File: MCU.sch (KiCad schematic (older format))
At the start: 10 parts, among them U2 TPS70925, U3 STM32L011F4Ux

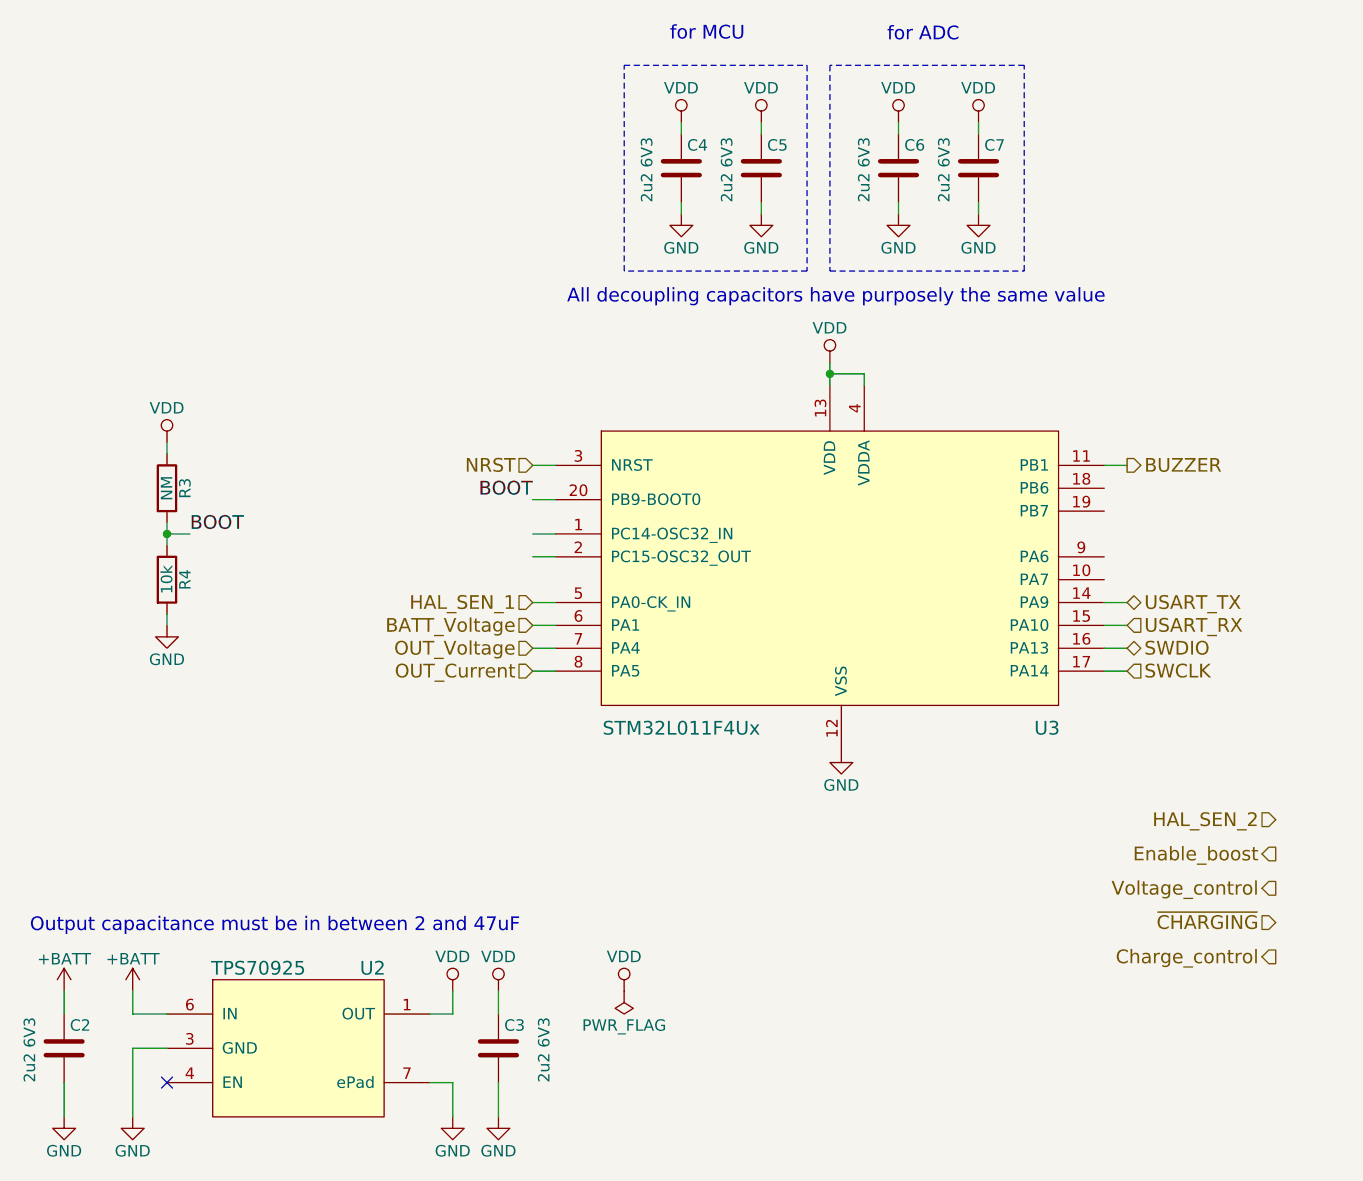
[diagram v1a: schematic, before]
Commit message: Updated MCU pinout
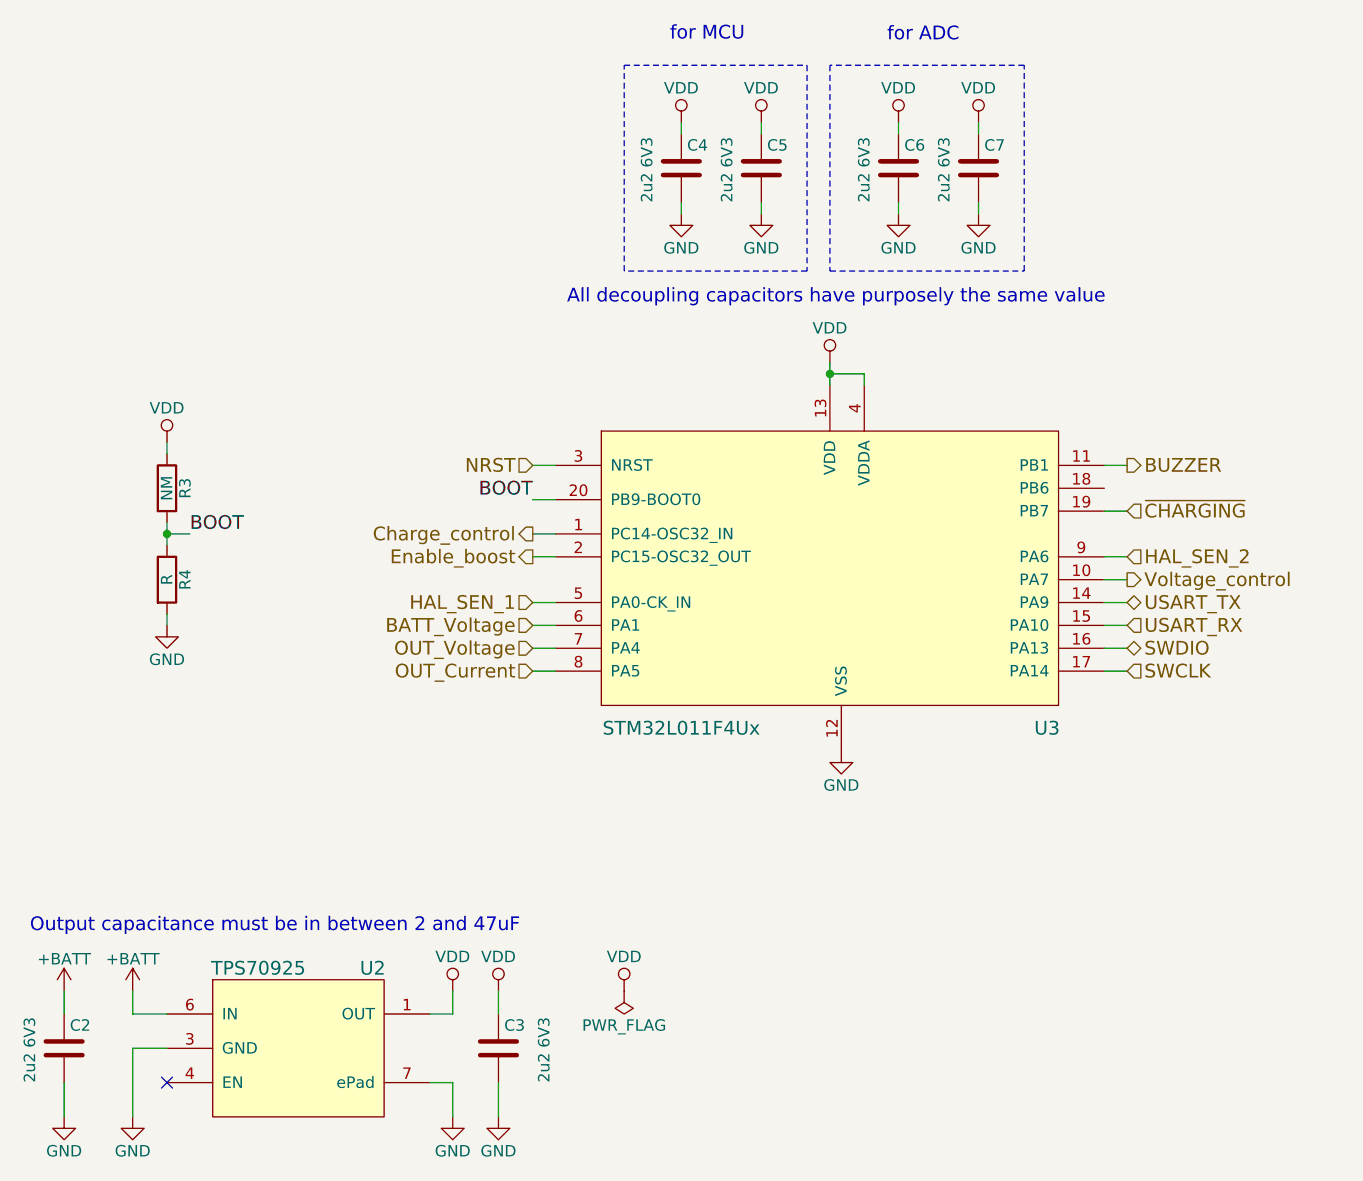
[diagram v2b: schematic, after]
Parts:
- R4: value 10k -> R
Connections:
- wire segments 40 -> 43
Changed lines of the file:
@@
 P 3200 4200
 F 0 "R4" V 3280 4200 50  0000 C CNN
-F 1 "10k" V 3200 4200 50  0000 C CNN
+F 1 "R" V 3200 4200 50  0000 C CNN
 F 2 "" V 3130 4200 50  0001 C CNN
 F 3 "" H 3200 4200 50  0001 C CNN
@@
 Wire Wire Line
 	4800 4300 4900 4300
-Text HLabel 8050 5250 0    60   Input ~ 0
+Text HLabel 7400 4100 2    60   Input ~ 0
 HAL_SEN_2
 $Comp
@@
 Text HLabel 7400 3700 2    60   Output ~ 0
 BUZZER
-Text HLabel 8050 5550 0    60   Output ~ 0
+Text HLabel 7400 4200 2    60   Output ~ 0
 Voltage_control
-Text HLabel 8050 5400 0    60   Output ~ 0
+Text HLabel 4800 4100 0    60   Output ~ 0
 Enable_boost
 Text HLabel 4800 4500 0    60   Input ~ 0
@@
 Text Notes 4950 3000 0    60   ~ 0
 All decoupling capacitors have purposely the same value\n
-Text HLabel 8050 5700 0    60   Input ~ 0
+Text HLabel 7400 3900 2    60   Input ~ 0
 ~CHARGING
-Text HLabel 8050 5850 0    60   Output ~ 0
+Text HLabel 4800 4000 0    60   Output ~ 0
 Charge_control
+Wire Wire Line
+	7300 4200 7400 4200
+Wire Wire Line
+	7300 4100 7400 4100
+Wire Wire Line
+	7300 3900 7400 3900
 $EndSCHEMATC

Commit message: Simplified schematic, changed pinout
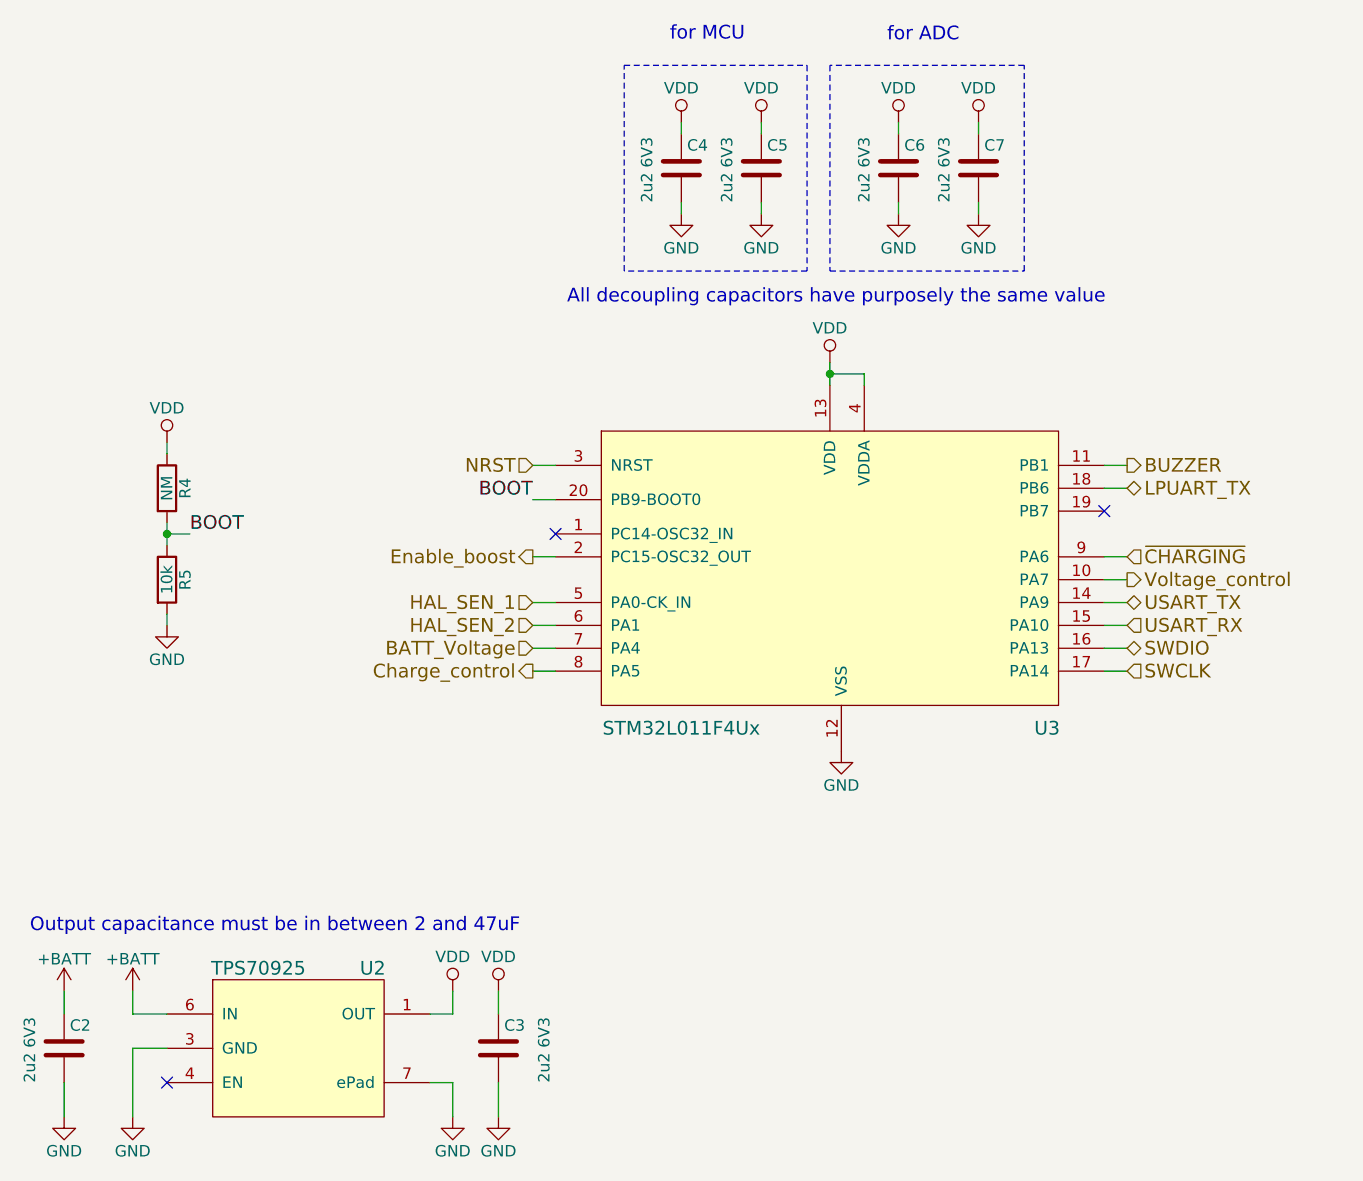
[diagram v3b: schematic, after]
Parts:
- C2, C3, C4, C5, C6, C7: footprint (none) -> Capacitors_SMD:C_0402
- R4: renamed from R3; footprint (none) -> Resistors_SMD:R_0402
- R5: renamed from R4; value R -> 10k; footprint (none) -> Resistors_SMD:R_0402
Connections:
- net OUT_Current is gone; now on net Charge_control: U3.8 (PA5)
- net OUT_Voltage is gone; now on net BATT_Voltage: U3.7 (PA4)
- net BATT_Voltage: no longer U3.6 (PA1)
- net Charge_control: no longer U3.1 (PC14-OSC32_IN)
- net HAL_SEN_2: now also U3.6 (PA1); no longer U3.9 (PA6)
- net ~CHARGING: now also U3.9 (PA6); no longer U3.19 (PB7)
- net LPUART_TX: now reaches U3.18 (PB6)
- no-connect marks 1 -> 3
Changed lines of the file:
@@
 $EndDescr
 $Comp
-L VDD #PWR30
+L VDD #PWR012
 U 1 1 5A9B30A9
 P 6100 3250
-F 0 "#PWR30" H 6100 3100 50  0001 C CNN
+F 0 "#PWR012" H 6100 3100 50  0001 C CNN
 F 1 "VDD" H 6100 3400 50  0000 C CNN
 F 2 "" H 6100 3250 50  0001 C CNN
@@
 Connection ~ 6100 3300
 $Comp
-L GND #PWR31
+L GND #PWR013
 U 1 1 5A9B30B3
 P 6150 4950
-F 0 "#PWR31" H 6150 4700 50  0001 C CNN
+F 0 "#PWR013" H 6150 4700 50  0001 C CNN
 F 1 "GND" H 6150 4800 50  0000 C CNN
 F 2 "" H 6150 4950 50  0001 C CNN
@@
 $EndComp
 $Comp
-L GND #PWR18
+L GND #PWR014
 U 1 1 5A9B3148
 P 3050 6550
-F 0 "#PWR18" H 3050 6300 50  0001 C CNN
+F 0 "#PWR014" H 3050 6300 50  0001 C CNN
 F 1 "GND" H 3050 6400 50  0000 C CNN
 F 2 "" H 3050 6550 50  0001 C CNN
@@
 NoConn ~ 3200 6400
 $Comp
-L GND #PWR22
+L GND #PWR015
 U 1 1 5A9B3188
 P 4450 6550
-F 0 "#PWR22" H 4450 6300 50  0001 C CNN
+F 0 "#PWR015" H 4450 6300 50  0001 C CNN
 F 1 "GND" H 4450 6400 50  0000 C CNN
 F 2 "" H 4450 6550 50  0001 C CNN
@@
 	4450 6400 4450 6550
 $Comp
-L VDD #PWR21
+L VDD #PWR016
 U 1 1 5A9B31B3
 P 4450 6000
-F 0 "#PWR21" H 4450 5850 50  0001 C CNN
+F 0 "#PWR016" H 4450 5850 50  0001 C CNN
 F 1 "VDD" H 4450 6150 50  0000 C CNN
 F 2 "" H 4450 6000 50  0001 C CNN
@@
 	4450 6100 4350 6100
 $Comp
-L +BATT #PWR17
+L +BATT #PWR017
 U 1 1 5A9B31F8
 P 3050 6000
-F 0 "#PWR17" H 3050 5850 50  0001 C CNN
+F 0 "#PWR017" H 3050 5850 50  0001 C CNN
 F 1 "+BATT" H 3050 6140 50  0000 C CNN
 F 2 "" H 3050 6000 50  0001 C CNN
@@
 F 0 "C3" H 4675 6350 50  0000 L CNN
 F 1 "2u2 6V3" V 4850 6100 50  0000 L CNN
-F 2 "" H 4688 6100 50  0001 C CNN
+F 2 "Capacitors_SMD:C_0402" H 4688 6100 50  0001 C CNN
 F 3 "" H 4650 6250 50  0001 C CNN
 	1    4650 6250
@@
 $EndComp
 $Comp
-L VDD #PWR23
+L VDD #PWR018
 U 1 1 5A9B32A8
 P 4650 6000
-F 0 "#PWR23" H 4650 5850 50  0001 C CNN
+F 0 "#PWR018" H 4650 5850 50  0001 C CNN
 F 1 "VDD" H 4650 6150 50  0000 C CNN
 F 2 "" H 4650 6000 50  0001 C CNN
@@
 $EndComp
 $Comp
-L GND #PWR24
+L GND #PWR019
 U 1 1 5A9B32D5
 P 4650 6550
-F 0 "#PWR24" H 4650 6300 50  0001 C CNN
+F 0 "#PWR019" H 4650 6300 50  0001 C CNN
 F 1 "GND" H 4650 6400 50  0000 C CNN
 F 2 "" H 4650 6550 50  0001 C CNN
@@
 F 0 "C2" H 2775 6350 50  0000 L CNN
 F 1 "2u2 6V3" V 2600 6100 50  0000 L CNN
-F 2 "" H 2788 6100 50  0001 C CNN
+F 2 "Capacitors_SMD:C_0402" H 2788 6100 50  0001 C CNN
 F 3 "" H 2750 6250 50  0001 C CNN
 	1    2750 6250
@@
 $EndComp
 $Comp
-L GND #PWR16
+L GND #PWR020
 U 1 1 5A9B33C8
 P 2750 6550
-F 0 "#PWR16" H 2750 6300 50  0001 C CNN
+F 0 "#PWR020" H 2750 6300 50  0001 C CNN
 F 1 "GND" H 2750 6400 50  0000 C CNN
 F 2 "" H 2750 6550 50  0001 C CNN
@@
 	2750 6400 2750 6550
 $Comp
-L +BATT #PWR15
+L +BATT #PWR021
 U 1 1 5A9B33E9
 P 2750 6000
-F 0 "#PWR15" H 2750 5850 50  0001 C CNN
+F 0 "#PWR021" H 2750 5850 50  0001 C CNN
 F 1 "+BATT" H 2750 6140 50  0000 C CNN
 F 2 "" H 2750 6000 50  0001 C CNN
@@
 F 0 "C4" H 5475 2500 50  0000 L CNN
 F 1 "2u2 6V3" V 5300 2250 50  0000 L CNN
-F 2 "" H 5488 2250 50  0001 C CNN
+F 2 "Capacitors_SMD:C_0402" H 5488 2250 50  0001 C CNN
 F 3 "" H 5450 2400 50  0001 C CNN
 	1    5450 2400
@@
 Output capacitance must be in between 2 and 47uF\n
 $Comp
-L VDD #PWR26
+L VDD #PWR022
 U 1 1 5A9B3944
 P 5450 2200
-F 0 "#PWR26" H 5450 2050 50  0001 C CNN
+F 0 "#PWR022" H 5450 2050 50  0001 C CNN
 F 1 "VDD" H 5450 2350 50  0000 C CNN
 F 2 "" H 5450 2200 50  0001 C CNN
@@
 	5450 2200 5450 2250
 $Comp
-L GND #PWR27
+L GND #PWR023
 U 1 1 5A9B3984
 P 5450 2600
-F 0 "#PWR27" H 5450 2350 50  0001 C CNN
+F 0 "#PWR023" H 5450 2350 50  0001 C CNN
 F 1 "GND" H 5450 2450 50  0000 C CNN
 F 2 "" H 5450 2600 50  0001 C CNN
@@
 F 0 "C5" H 5825 2500 50  0000 L CNN
 F 1 "2u2 6V3" V 5650 2250 50  0000 L CNN
-F 2 "" H 5838 2250 50  0001 C CNN
+F 2 "Capacitors_SMD:C_0402" H 5838 2250 50  0001 C CNN
 F 3 "" H 5800 2400 50  0001 C CNN
 	1    5800 2400
@@
 $EndComp
 $Comp
-L VDD #PWR28
+L VDD #PWR024
 U 1 1 5A9B39F3
 P 5800 2200
-F 0 "#PWR28" H 5800 2050 50  0001 C CNN
+F 0 "#PWR024" H 5800 2050 50  0001 C CNN
 F 1 "VDD" H 5800 2350 50  0000 C CNN
 F 2 "" H 5800 2200 50  0001 C CNN
@@
 	5800 2200 5800 2250
 $Comp
-L GND #PWR29
+L GND #PWR025
 U 1 1 5A9B39FA
 P 5800 2600
-F 0 "#PWR29" H 5800 2350 50  0001 C CNN
+F 0 "#PWR025" H 5800 2350 50  0001 C CNN
 F 1 "GND" H 5800 2450 50  0000 C CNN
 F 2 "" H 5800 2600 50  0001 C CNN
@@
 F 0 "C6" H 6425 2500 50  0000 L CNN
 F 1 "2u2 6V3" V 6250 2250 50  0000 L CNN
-F 2 "" H 6438 2250 50  0001 C CNN
+F 2 "Capacitors_SMD:C_0402" H 6438 2250 50  0001 C CNN
 F 3 "" H 6400 2400 50  0001 C CNN
 	1    6400 2400
@@
 $EndComp
 $Comp
-L VDD #PWR32
+L VDD #PWR026
 U 1 1 5A9B3B2B
 P 6400 2200
-F 0 "#PWR32" H 6400 2050 50  0001 C CNN
+F 0 "#PWR026" H 6400 2050 50  0001 C CNN
 F 1 "VDD" H 6400 2350 50  0000 C CNN
 F 2 "" H 6400 2200 50  0001 C CNN
@@
 	6400 2200 6400 2250
 $Comp
-L GND #PWR33
+L GND #PWR027
 U 1 1 5A9B3B32
 P 6400 2600
-F 0 "#PWR33" H 6400 2350 50  0001 C CNN
+F 0 "#PWR027" H 6400 2350 50  0001 C CNN
 F 1 "GND" H 6400 2450 50  0000 C CNN
 F 2 "" H 6400 2600 50  0001 C CNN
@@
 F 0 "C7" H 6775 2500 50  0000 L CNN
 F 1 "2u2 6V3" V 6600 2250 50  0000 L CNN
-F 2 "" H 6788 2250 50  0001 C CNN
+F 2 "Capacitors_SMD:C_0402" H 6788 2250 50  0001 C CNN
 F 3 "" H 6750 2400 50  0001 C CNN
 	1    6750 2400
@@
 $EndComp
 $Comp
-L VDD #PWR34
+L VDD #PWR028
 U 1 1 5A9B3B8A
 P 6750 2200
-F 0 "#PWR34" H 6750 2050 50  0001 C CNN
+F 0 "#PWR028" H 6750 2050 50  0001 C CNN
 F 1 "VDD" H 6750 2350 50  0000 C CNN
 F 2 "" H 6750 2200 50  0001 C CNN
@@
 	6750 2200 6750 2250
 $Comp
-L GND #PWR35
+L GND #PWR029
 U 1 1 5A9B3B91
 P 6750 2600
-F 0 "#PWR35" H 6750 2350 50  0001 C CNN
+F 0 "#PWR029" H 6750 2350 50  0001 C CNN
 F 1 "GND" H 6750 2450 50  0000 C CNN
 F 2 "" H 6750 2600 50  0001 C CNN
@@
 	7300 4500 7400 4500
 $Comp
-L R R4
+L R R5
 U 1 1 5A9B431F
 P 3200 4200
-F 0 "R4" V 3280 4200 50  0000 C CNN
-F 1 "R" V 3200 4200 50  0000 C CNN
-F 2 "" V 3130 4200 50  0001 C CNN
+F 0 "R5" V 3280 4200 50  0000 C CNN
+F 1 "10k" V 3200 4200 50  0000 C CNN
+F 2 "Resistors_SMD:R_0402" V 3130 4200 50  0001 C CNN
 F 3 "" H 3200 4200 50  0001 C CNN
 	1    3200 4200
@@
 $EndComp
 $Comp
-L R R3
+L R R4
 U 1 1 5A9B4434
 P 3200 3800
-F 0 "R3" V 3280 3800 50  0000 C CNN
+F 0 "R4" V 3280 3800 50  0000 C CNN
 F 1 "NM" V 3200 3800 50  0000 C CNN
-F 2 "" V 3130 3800 50  0001 C CNN
+F 2 "Resistors_SMD:R_0402" V 3130 3800 50  0001 C CNN
 F 3 "" H 3200 3800 50  0001 C CNN
 	1    3200 3800
@@
 $EndComp
 $Comp
-L VDD #PWR19
+L VDD #PWR030
 U 1 1 5A9B4476
 P 3200 3600
-F 0 "#PWR19" H 3200 3450 50  0001 C CNN
+F 0 "#PWR030" H 3200 3450 50  0001 C CNN
 F 1 "VDD" H 3200 3750 50  0000 C CNN
 F 2 "" H 3200 3600 50  0001 C CNN
@@
 	3200 3650 3200 3600
 $Comp
-L GND #PWR20
+L GND #PWR031
 U 1 1 5A9B4528
 P 3200 4400
-F 0 "#PWR20" H 3200 4150 50  0001 C CNN
+F 0 "#PWR031" H 3200 4150 50  0001 C CNN
 F 1 "GND" H 3200 4250 50  0000 C CNN
 F 2 "" H 3200 4400 50  0001 C CNN
@@
 Wire Wire Line
 	4800 4300 4900 4300
-Text HLabel 7400 4100 2    60   Input ~ 0
+Text HLabel 4800 4400 0    60   Input ~ 0
 HAL_SEN_2
-$Comp
-L PWR_FLAG #FLG3
-U 1 1 5AA0AD8D
-P 5200 6000
-F 0 "#FLG3" H 5200 6075 50  0001 C CNN
-F 1 "PWR_FLAG" H 5200 6150 50  0000 C CNN
-F 2 "" H 5200 6000 50  0001 C CNN
-F 3 "" H 5200 6000 50  0001 C CNN
-	1    5200 6000
-	-1   0    0    1
-$EndComp
-$Comp
-L VDD #PWR25
-U 1 1 5AA0ADBD
-P 5200 6000
-F 0 "#PWR25" H 5200 5850 50  0001 C CNN
-F 1 "VDD" H 5200 6150 50  0000 C CNN
-F 2 "" H 5200 6000 50  0001 C CNN
-F 3 "" H 5200 6000 50  0001 C CNN
-	1    5200 6000
-	1    0    0    -1
-$EndComp
 Text HLabel 7400 3700 2    60   Output ~ 0
 BUZZER
@@
 Text HLabel 4800 4100 0    60   Output ~ 0
 Enable_boost
+Wire Wire Line
+	4800 4500 4900 4500
 Text HLabel 4800 4500 0    60   Input ~ 0
-OUT_Voltage
-Text HLabel 4800 4600 0    60   Input ~ 0
-OUT_Current
-Wire Wire Line
-	4800 4400 4900 4400
-Wire Wire Line
-	4800 4500 4900 4500
+BATT_Voltage
+Wire Wire Line
+	7300 3700 7400 3700
 Wire Wire Line
 	4800 4600 4900 4600
-Text HLabel 4800 4400 0    60   Input ~ 0
-BATT_Voltage
-Wire Wire Line
-	7300 3700 7400 3700
-Wire Wire Line
-	4800 4000 4900 4000
 Wire Wire Line
 	4800 4100 4900 4100
+$Comp
+L TPS709 U2
+U 1 1 5AA7A66F
+P 3800 6250
+F 0 "U2" H 4100 6600 60  0000 C CNN
+F 1 "TPS70925" H 3600 6600 60  0000 C CNN
+F 2 "lakotamm-miscellaneous:WSON-6_2x2mm_Pitch0.65mm" H 3850 5600 60  0001 C CNN
+F 3 "http://www.ti.com/lit/ds/symlink/tps709.pdf" H 3800 5750 60  0001 C CNN
+F 4 "TPS70925DBV" H 3800 6600 60  0001 C CNN "MPN"
+	1    3800 6250
+	1    0    0    -1
+$EndComp
+Text Notes 4950 3000 0    60   ~ 0
+All decoupling capacitors have purposely the same value\n
+Text HLabel 7400 4100 2    60   Input ~ 0
+~CHARGING
+Text HLabel 4800 4600 0    60   Output ~ 0
+Charge_control
+Wire Wire Line
+	7300 4200 7400 4200
+Wire Wire Line
+	4900 4400 4800 4400
+Wire Wire Line
+	7400 4100 7300 4100
+Text HLabel 7400 3800 2    60   BiDi ~ 0
+LPUART_TX
+Wire Wire Line
+	7300 3800 7400 3800
+NoConn ~ 7300 3900
 $Comp
 L STM32L011F4Ux U3
@@
 	1    0    0    -1
 $EndComp
-$Comp
-L TPS709 U2
-U 1 1 5AA7A66F
-P 3800 6250
-F 0 "U2" H 4100 6600 60  0000 C CNN
-F 1 "TPS70925" H 3600 6600 60  0000 C CNN
-F 2 "lakotamm-miscellaneous:WSON-6_2x2mm_Pitch0.65mm" H 3850 5600 60  0001 C CNN
-F 3 "http://www.ti.com/lit/ds/symlink/tps709.pdf" H 3800 5750 60  0001 C CNN
-F 4 "TPS70925DBV" H 3800 6600 60  0001 C CNN "MPN"
-	1    3800 6250
-	1    0    0    -1
-$EndComp
-Text Notes 4950 3000 0    60   ~ 0
-All decoupling capacitors have purposely the same value\n
-Text HLabel 7400 3900 2    60   Input ~ 0
-~CHARGING
-Text HLabel 4800 4000 0    60   Output ~ 0
-Charge_control
-Wire Wire Line
-	7300 4200 7400 4200
-Wire Wire Line
-	7300 4100 7400 4100
-Wire Wire Line
-	7300 3900 7400 3900
+NoConn ~ 4900 4000
 $EndSCHEMATC
